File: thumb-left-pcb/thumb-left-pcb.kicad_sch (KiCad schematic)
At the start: 25 parts, among them J1 Conn_01x10

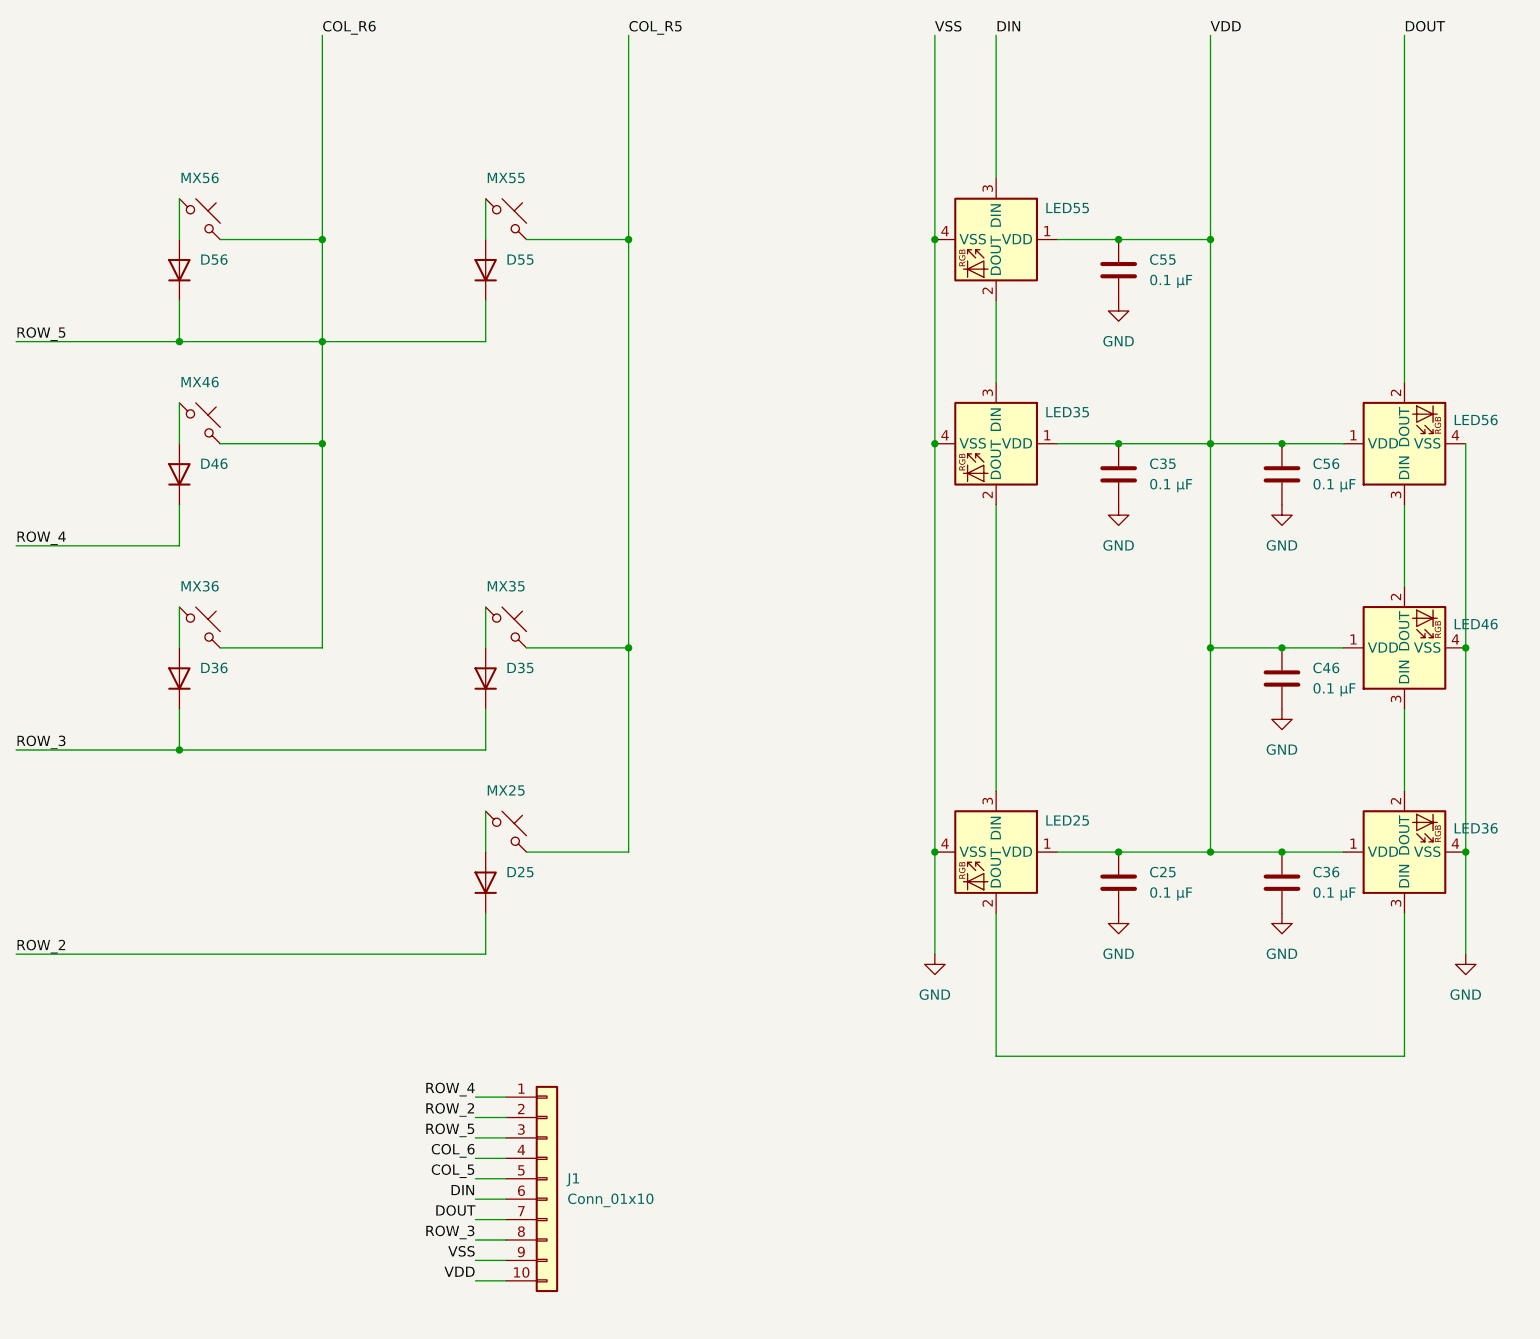
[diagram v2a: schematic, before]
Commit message: fixed net names for left thumb columns
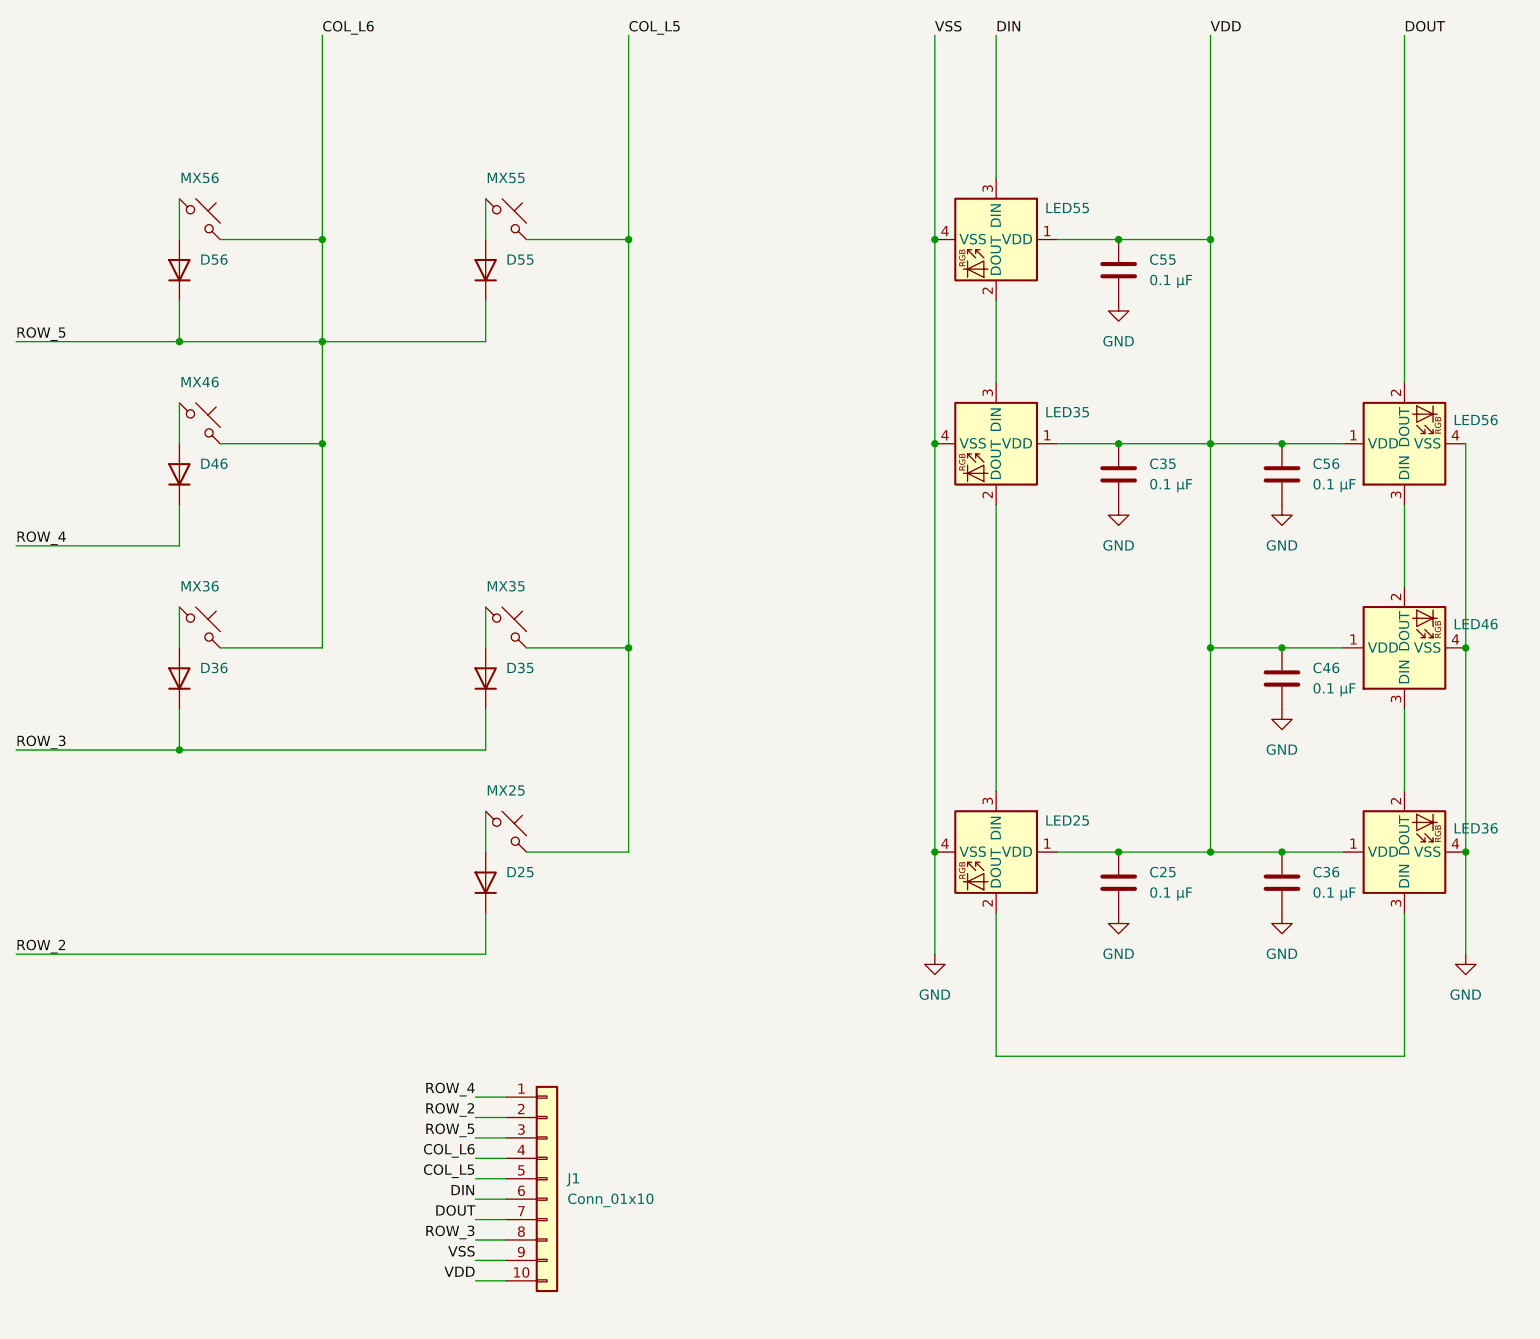
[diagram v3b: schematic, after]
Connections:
- net COL_R5 is gone; now on net COL_L5: MX25.2, MX35.2, MX55.2
- net COL_R6 is gone; now on net COL_L6: D55.1 (K), D56.1 (K), J1.3 (Pin_3), MX36.2, MX46.2, MX56.2
- net COL_5 renamed COL_L5
- net COL_6 renamed COL_L6
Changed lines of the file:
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@@
 		)
 	)
-	(label "COL_R5"
+	(label "COL_L5"
 		(at 114.3 25.4 0)
 		(effects
@@
 		)
 	)
-	(label "COL_6"
+	(label "COL_L6"
 		(at 95.25 165.1 180)
 		(effects
@@
 		)
 	)
-	(label "COL_5"
+	(label "COL_L5"
 		(at 95.25 167.64 180)
 		(effects
@@
 		)
 	)
-	(label "COL_R6"
+	(label "COL_L6"
 		(at 76.2 25.4 0)
 		(effects

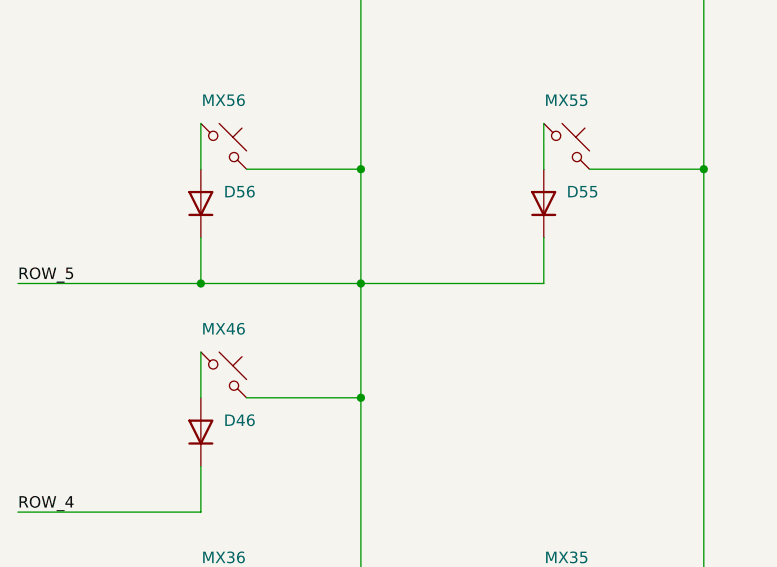
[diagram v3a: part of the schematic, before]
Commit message: fix left thumb nets
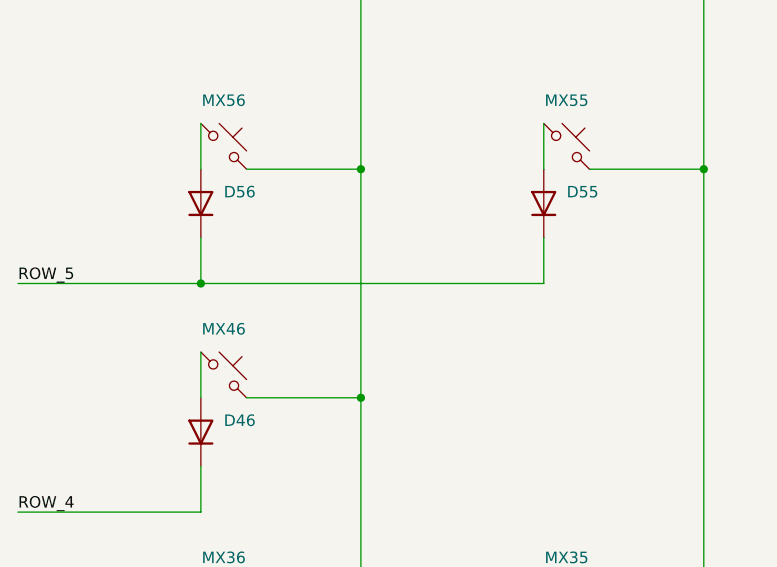
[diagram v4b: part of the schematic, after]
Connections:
- net COL_L6: no longer D55.1 (K), D56.1 (K), J1.3 (Pin_3)
- new net ROW_5: D55.1 (K), D56.1 (K), J1.3 (Pin_3)
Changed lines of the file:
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@@
+	)
+	(junction
+		(at 186.69 50.8)
+		(diameter 0)
+		(color 0 0 0 0)
+	)
+	(junction
+		(at 175.26 50.8)
+		(diameter 0)
+		(color 0 0 0 0)
+	)
+	(junction
+		(at 114.3 50.8)
+		(diameter 0)
+		(color 0 0 0 0)
+	)
+	(junction
+		(at 186.69 76.2)
+		(diameter 0)
+		(color 0 0 0 0)
+	)
+	(junction
+		(at 218.44 127)
+		(diameter 0)
+		(color 0 0 0 0)
+	)
+	(junction
+		(at 186.69 101.6)
+		(diameter 0)
+		(color 0 0 0 0)
 	)
 	(junction
@@
 	)
 	(junction
-		(at 186.69 50.8)
-		(diameter 0)
-		(color 0 0 0 0)
-	)
-	(junction
-		(at 175.26 50.8)
-		(diameter 0)
-		(color 0 0 0 0)
-	)
-	(junction
-		(at 76.2 63.5)
-		(diameter 0)
-		(color 0 0 0 0)
-	)
-	(junction
-		(at 114.3 50.8)
-		(diameter 0)
-		(color 0 0 0 0)
-	)
-	(junction
-		(at 186.69 76.2)
-		(diameter 0)
-		(color 0 0 0 0)
-	)
-	(junction
-		(at 218.44 127)
-		(diameter 0)
-		(color 0 0 0 0)
-	)
-	(junction
-		(at 186.69 101.6)
-		(diameter 0)
-		(color 0 0 0 0)
-	)
-	(junction
 		(at 152.4 50.8)
 		(diameter 0)
@@
 	(wire
 		(pts
-			(xy 58.42 63.5) (xy 76.2 63.5)
-		)
-		(stroke
-			(width 0)
-			(type default)
-		)
-	)
-	(wire
-		(pts
-			(xy 76.2 50.8) (xy 76.2 63.5)
+			(xy 58.42 63.5) (xy 96.52 63.5)
 		)
 		(stroke
@@
 	(wire
 		(pts
-			(xy 76.2 63.5) (xy 76.2 76.2)
+			(xy 76.2 50.8) (xy 76.2 76.2)
 		)
 		(stroke
@@
 		)
 		(stroke
-			(width 0)
-			(type default)
-		)
-	)
-	(wire
-		(pts
-			(xy 76.2 63.5) (xy 96.52 63.5)
-		)
-		(stroke
